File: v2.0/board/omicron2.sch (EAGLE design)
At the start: 195 parts, among them IC1 XC6SLX4-1876221, IC2 TPS73033DBV-1135395, IC3 LD6806TD/12H-2095494, IC4 H57V2562GTR-75C-1907383, IC5 M25P40-2253716, IC6 TPS73033DBV-1135395, Q1 PDTC123-1757992, Q2 BC807W, Q3 PDTC123-1757992, Q4 BC807W, X1 USB-MICRO-B-BOTTOM, X2 7C-33.3-1842039

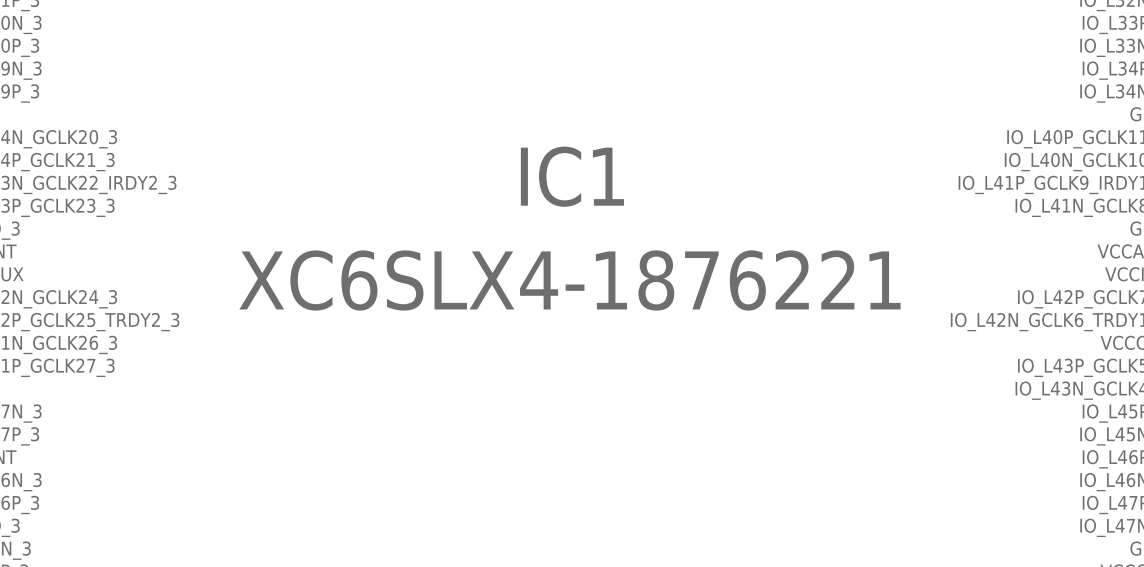
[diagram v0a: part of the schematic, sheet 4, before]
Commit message: Changed the device to 6slx9; added board errata
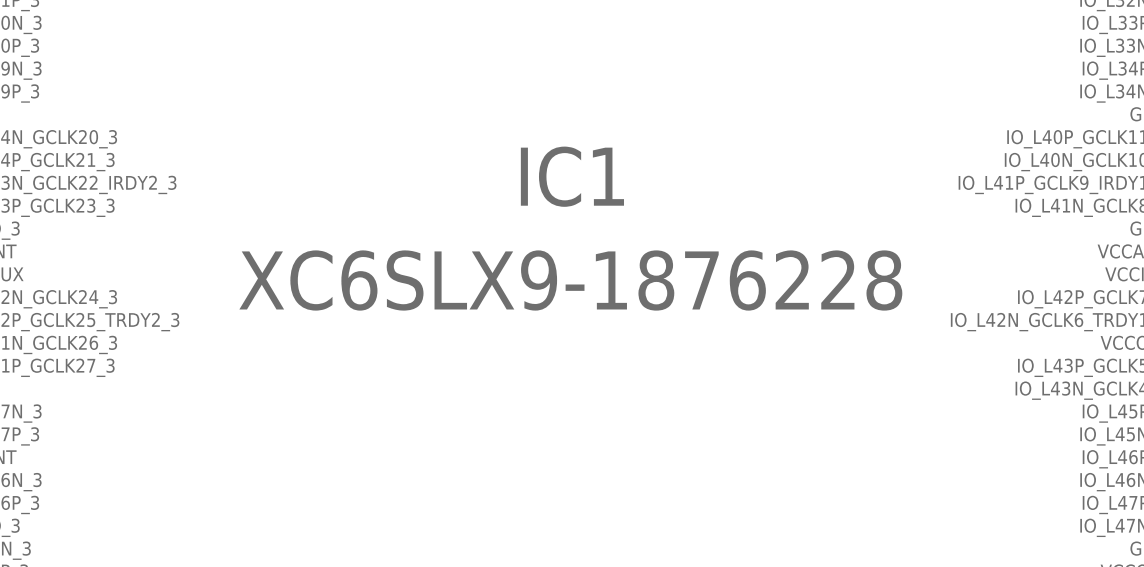
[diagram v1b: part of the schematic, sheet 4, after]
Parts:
- IC1: value XC6SLX4-1876221 -> XC6SLX9-1876228
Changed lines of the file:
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@@
 <?xml version="1.0" encoding="utf-8"?>
 <!DOCTYPE eagle SYSTEM "eagle.dtd">
-<eagle version="6.3">
+<eagle version="7.0.0">
 <drawing>
 <settings>
@@
 </classes>
 <parts>
-<part name="IC1" library="xilinx" deviceset="XC6SLX4*" device="TQG144" technology="-2" value="XC6SLX4-1876221"/>
+<part name="IC1" library="xilinx" deviceset="XC6SLX4*" device="TQG144" technology="-2" value="XC6SLX9-1876228"/>
 <part name="GND1" library="supply1" deviceset="GND" device=""/>
 <part name="GND2" library="supply1" deviceset="GND" device=""/>
